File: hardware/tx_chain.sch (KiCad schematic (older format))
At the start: 34 parts

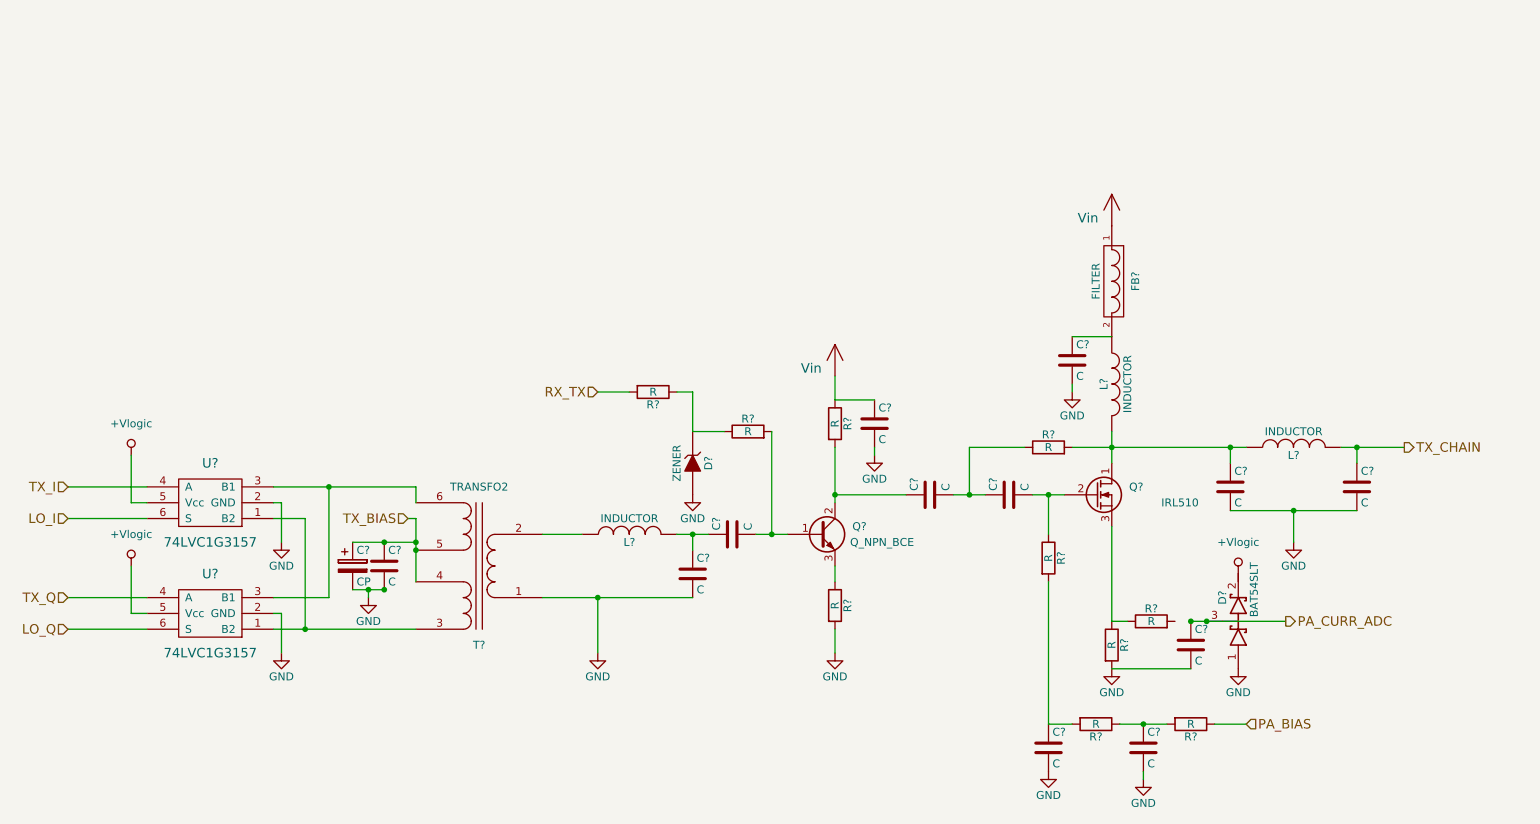
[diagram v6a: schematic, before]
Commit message: Fixed broken wire in tx_chain.sch
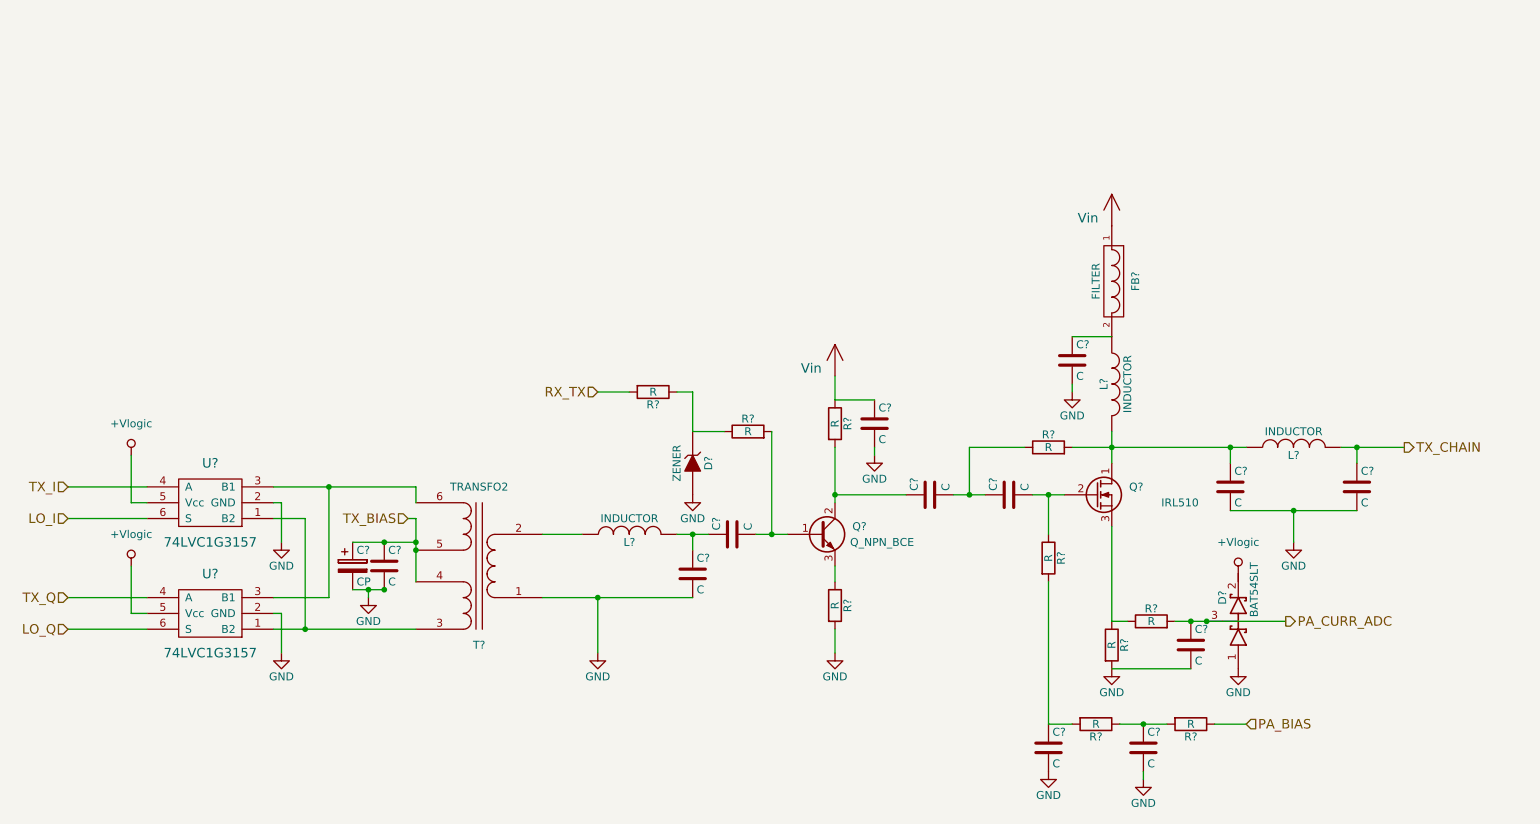
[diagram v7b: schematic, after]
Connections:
- net PA_CURR_ADC: now also R?.2
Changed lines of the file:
@@
 	3250 3950 3250 4650
 Wire Wire Line
-	3050 4650 3250 4650
-Wire Wire Line
-	3250 4650 3950 4650
+	3050 4650 3950 4650
 Wire Wire Line
 	3050 4450 3400 4450
@@
 	3400 4450 3400 3750
 Wire Wire Line
-	3050 3750 3400 3750
-Wire Wire Line
-	3400 3750 3950 3750
+	3050 3750 3950 3750
 Wire Wire Line
 	3050 3850 3100 3850
@@
 Connection ~ 3250 4650
 Wire Wire Line
-	3550 4100 3750 4100
+	3550 4100 3950 4100
 Wire Wire Line
-	3750 4100 3950 4100
-Wire Wire Line
-	3950 3950 3950 4100
-Wire Wire Line
-	3950 4100 3950 4150
-Wire Wire Line
-	3950 4150 3950 4350
+	3950 3950 3950 4350
 Connection ~ 3750 4100
 Connection ~ 3750 4400
@@
 	4750 4050 5000 4050
 Wire Wire Line
-	4750 4450 5100 4450
-Wire Wire Line
-	5100 4450 5700 4450
+	4750 4450 5700 4450
 Wire Wire Line
 	5700 4150 5700 4050
 Wire Wire Line
-	5600 4050 5700 4050
-Wire Wire Line
-	5700 4050 5800 4050
+	5600 4050 5800 4050
 Connection ~ 5700 4050
 Wire Wire Line
-	6100 4050 6200 4050
-Wire Wire Line
-	6200 4050 6300 4050
+	6100 4050 6300 4050
 Wire Wire Line
 	5100 4800 5100 4450
@@
 	6850 3500 6850 3550
 Wire Wire Line
-	6600 3500 6600 3800
-Wire Wire Line
-	6600 3800 6600 3850
+	6600 3500 6600 3850
 Wire Wire Line
 	7050 3800 6600 3800
 Connection ~ 6600 3800
 Wire Wire Line
-	7850 3800 7950 3800
-Wire Wire Line
-	7950 3800 8050 3800
+	7850 3800 8050 3800
 Wire Wire Line
 	7950 3800 7950 4050
 Wire Wire Line
-	7350 3800 7450 3800
-Wire Wire Line
-	7450 3800 7550 3800
+	7350 3800 7550 3800
 Wire Wire Line
 	7800 3500 7450 3500
@@
 Connection ~ 7950 3800
 Wire Wire Line
-	8100 3500 8350 3500
+	8100 3500 9200 3500
 Wire Wire Line
-	8350 3500 9100 3500
-Wire Wire Line
-	9100 3500 9200 3500
-Wire Wire Line
-	8350 3400 8350 3500
-Wire Wire Line
-	8350 3500 8350 3600
+	8350 3400 8350 3600
 Wire Wire Line
 	8100 3100 8100 3150
@@
 Connection ~ 9900 3500
 Wire Wire Line
-	9100 3900 9500 3900
-Wire Wire Line
-	9500 3900 9900 3900
+	9100 3900 9900 3900
 Wire Wire Line
 	9500 4100 9500 3900
@@
 	7950 5250 8100 5250
 Wire Wire Line
-	9800 3500 9900 3500
-Wire Wire Line
-	9900 3500 10200 3500
+	9800 3500 10200 3500
 Wire Wire Line
 	6200 3400 6200 4050
@@
 	5700 3400 5700 3150
 Wire Wire Line
-	3550 4400 3650 4400
-Wire Wire Line
-	3650 4400 3750 4400
+	3550 4400 3750 4400
 Connection ~ 3950 4150
 Wire Wire Line
@@
 	8550 5600 8550 5550
 Wire Wire Line
-	8400 5250 8550 5250
-Wire Wire Line
-	8550 5250 8700 5250
+	8400 5250 8700 5250
 Connection ~ 8550 5250
 Wire Wire Line
@@
 	5100 3150 5300 3150
 Wire Wire Line
-	8850 4600 8950 4600
-Wire Wire Line
-	8950 4600 9450 4600
+	8750 4600 9450 4600
 Connection ~ 8950 4600
 $Comp

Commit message: fixed some bugs
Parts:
- removed D?: BAT54SLT, symbol D_Schottky_x2_Serial_AKC
- added R?: 100k, symbol R
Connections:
- net GND: now also R?.2
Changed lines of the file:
@@
 Text HLabel 9450 4600 2    60   Output ~ 0
 PA_CURR_ADC
-$Comp
-L +Vlogic #PWR032
-U 1 1 57E47CF4
-P 9150 4300
-F 0 "#PWR032" H 9150 4100 50  0001 C CNN
-F 1 "+Vlogic" H 9150 4500 50  0000 C CNN
-F 2 "" H 9150 4300 50  0000 C CNN
-F 3 "" H 9150 4300 50  0000 C CNN
-	1    9150 4300
-	1    0    0    -1
-$EndComp
-$Comp
-L GND #PWR033
-U 1 1 57E47E8B
-P 9150 4900
-F 0 "#PWR033" H 9150 4650 50  0001 C CNN
-F 1 "GND" H 9150 4750 50  0000 C CNN
-F 2 "" H 9150 4900 50  0000 C CNN
-F 3 "" H 9150 4900 50  0000 C CNN
-	1    9150 4900
-	1    0    0    -1
-$EndComp
 Text HLabel 3900 3950 0    60   Input ~ 0
 TX_BIAS
@@
 Text HLabel 5100 3150 0    60   Input ~ 0
 RX_TX
-$Comp
-L D_Schottky_x2_Serial_AKC D?
-U 1 1 57ECEB79
-P 9150 4600
-F 0 "D?" H 9300 4500 50  0000 C CNN
-F 1 "BAT54SLT" H 9350 4700 50  0000 C CNN
-F 2 "" H 9150 4600 50  0000 C CNN
-F 3 "" H 9150 4600 50  0000 C CNN
-	1    9150 4600
-	0    1    -1   0
-$EndComp
 Wire Wire Line
 	3050 3950 3250 3950
@@
 Wire Wire Line
 	8750 4600 9450 4600
-Connection ~ 8950 4600
 $Comp
 L FILTER FB?
@@
 	0    1    1    0
 $EndComp
+$Comp
+L R R?
+U 1 1 57EAC331
+P 9100 5400
+F 0 "R?" V 9180 5400 50  0000 C CNN
+F 1 "100k" V 9100 5400 50  0000 C CNN
+F 2 "" V 9030 5400 50  0000 C CNN
+F 3 "" H 9100 5400 50  0000 C CNN
+	1    9100 5400
+	1    0    0    -1
+$EndComp
+$Comp
+L GND #PWR?
+U 1 1 57EAC40D
+P 9100 5600
+F 0 "#PWR?" H 9100 5350 50  0001 C CNN
+F 1 "GND" H 9100 5450 50  0000 C CNN
+F 2 "" H 9100 5600 50  0000 C CNN
+F 3 "" H 9100 5600 50  0000 C CNN
+	1    9100 5600
+	1    0    0    -1
+$EndComp
+Wire Wire Line
+	9100 5600 9100 5550
 $EndSCHEMATC
